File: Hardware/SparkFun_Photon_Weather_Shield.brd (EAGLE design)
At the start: 66 x 35.6 mm, 43 parts, among them U1 3.3V MIC5219, U2 HTU21D, U3 MPL3115A2LGA8

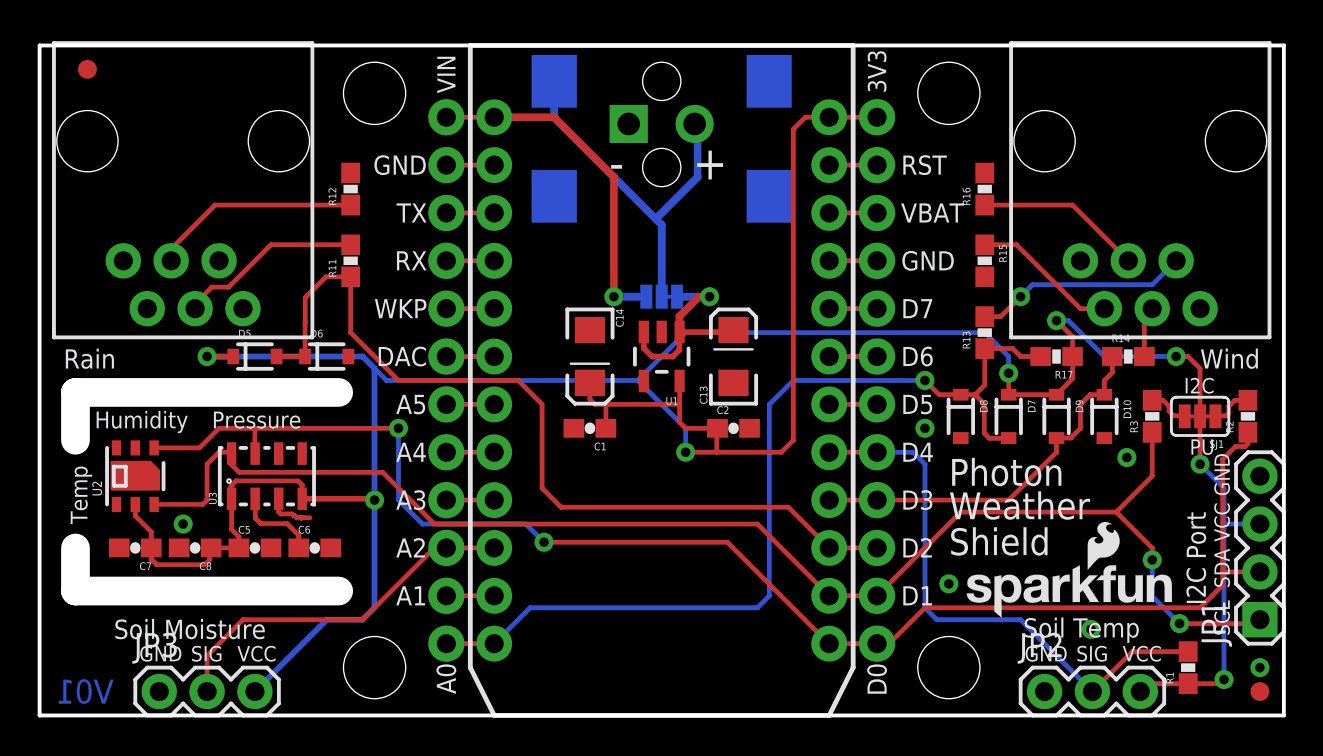
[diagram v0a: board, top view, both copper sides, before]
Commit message: Peer Review complete
Peer review with Jim, added 3.3V disable jumper for two power sources
at once (debugging), minor edits.
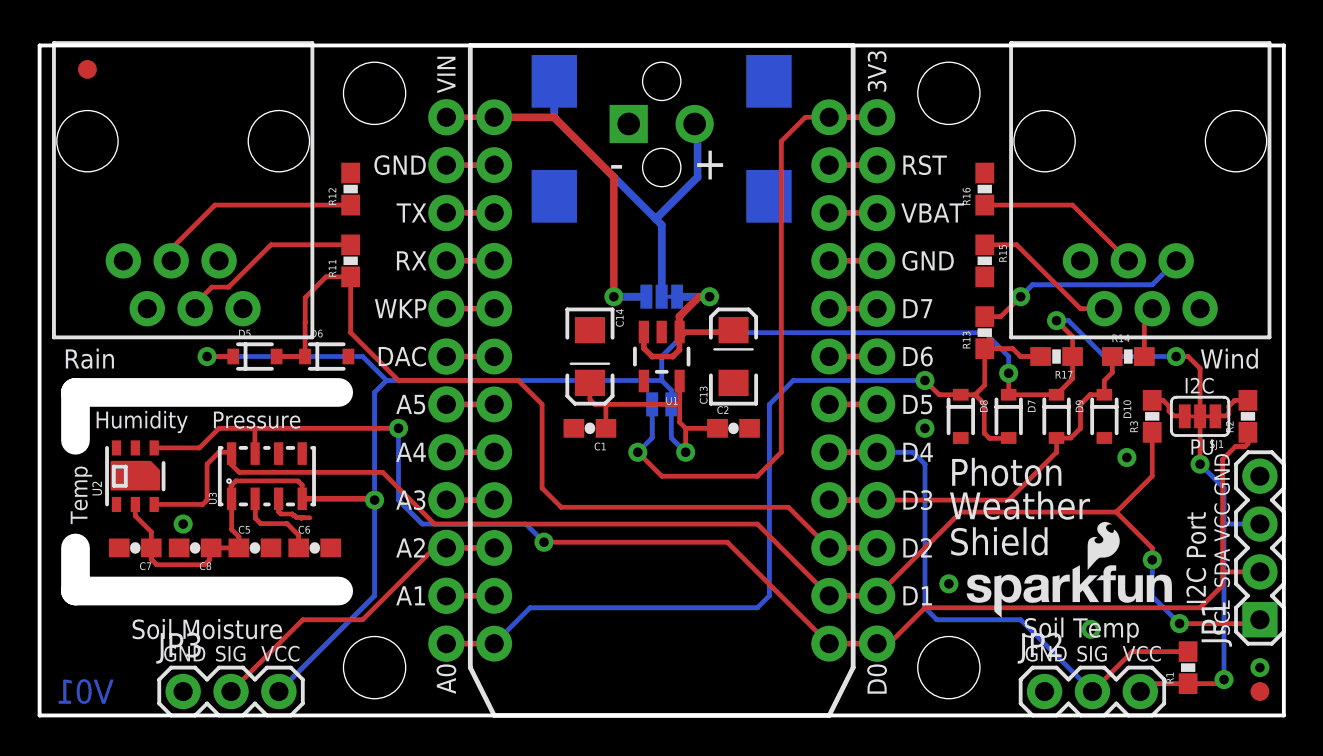
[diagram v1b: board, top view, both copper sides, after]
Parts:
- added SJ3: (no value), SparkFun-Passives:PAD-JUMPER-2-NC_BY_TRACE_YES_SILK
- moved U$1 24.2 mm to (15.2, 10.2)
- moved LOGO1 21.6 mm to (54.6, 12.1)
- moved JP3 1.27 mm to (7.62, 1.27)
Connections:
- new net N$7: JP4.24, JP4.3V3, SJ3.1
- net 3.3V: now also SJ3.2; no longer JP4.24, JP4.3V3
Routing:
- net N$7: track 0.00 -> 31.1 mm, vias 0 -> 1
- net 3.3V: track 171.7 -> 145.2 mm
- net SOIL_MOIST: track 17.0 -> 14.6 mm
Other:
- board text added: "3.3V Disable"
